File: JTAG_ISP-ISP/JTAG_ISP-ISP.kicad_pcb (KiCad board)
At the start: 2 copper layers, 23.1 x 46.1 mm, 11 parts, among them J1 Conn_02x03_Counter_Clockwise, J2 Conn_01x08, J3 Conn_01x08

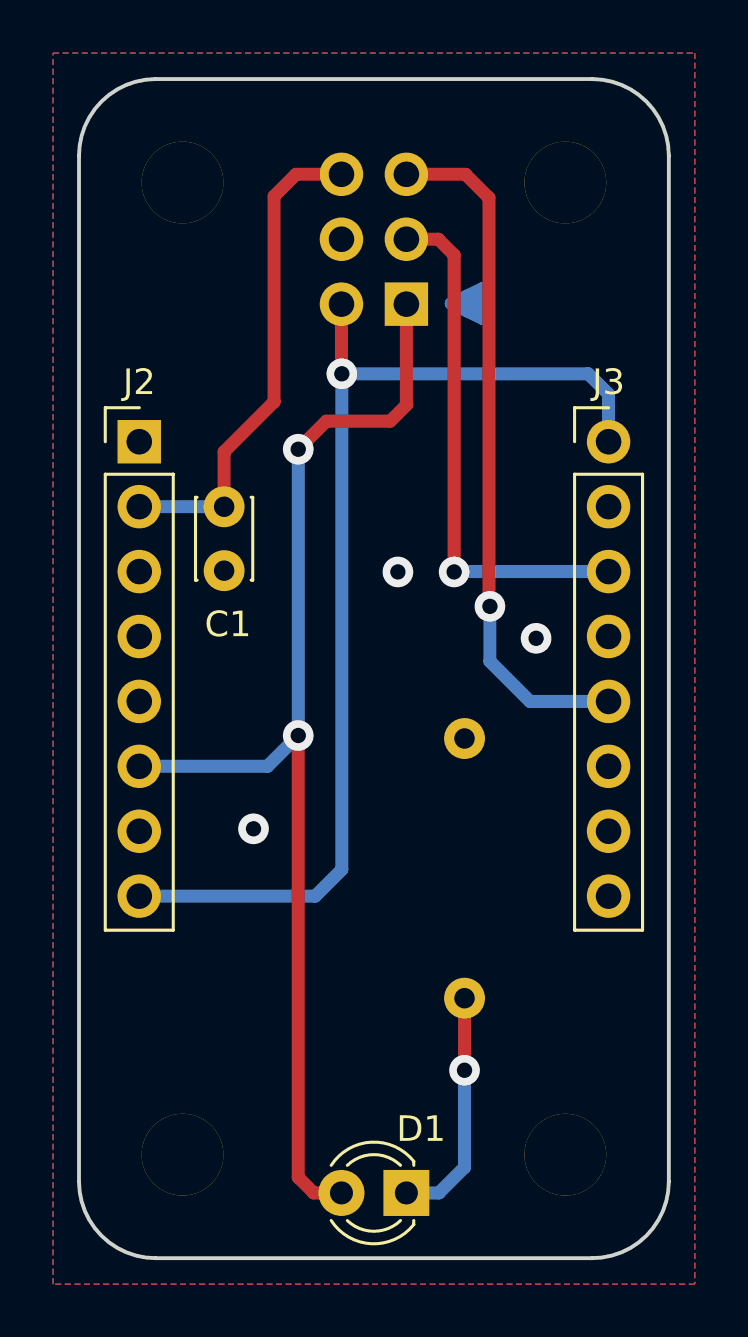
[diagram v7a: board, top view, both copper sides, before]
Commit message: # [PCB] * Correction mauvaise numérotation de broche sur le header J1 du projet ISP. * Correction de mauvaise couche pour les piste du condo C1 et de la DEL D1 du projet ISP. * Projet ISP routé à nouveau. * Utilisation de trous de montage avec pads. + Ajout de GND et de VCC dans le projet ISP sur les broches non utilisés de J2 & J3. * Mise à jours de la cartouche pour les 2 projets.     * Date actuelle;     * Version actuelle;     * Titre du projet.
# [SCHÉMA]
* Correction mauvaise numérotation de broche sur le header J1 du projet ISP.
+ Ajout de GND et de VCC dans le projet ISP sur les broches non utilisés de J2 & J3.
    + Ajout des nouveaux nom de broche sur J2 & J3.
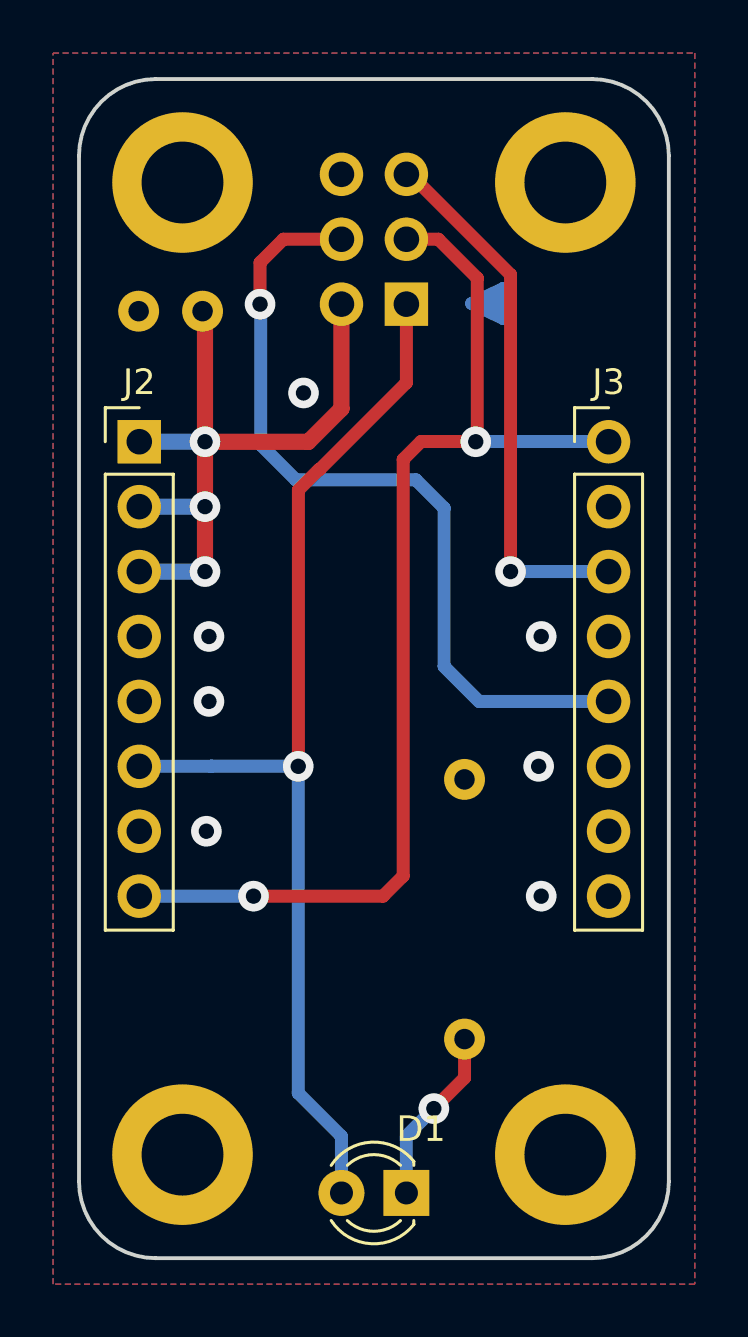
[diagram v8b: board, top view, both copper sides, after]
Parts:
- removed the REF** at (163.8, 103.4)
- removed the REF** at (163.8, 65.4)
- removed the REF** at (148.9, 103.4)
- removed the REF** at (148.9, 65.4)
- added REF**: MountingHole_3.2mm_M3_ISO14580_Pad, MountingHole:MountingHole_3.2mm_M3_ISO14580_Pad, F.Cu at (148.9, 65.4)
- added REF**: MountingHole_3.2mm_M3_ISO14580_Pad, MountingHole:MountingHole_3.2mm_M3_ISO14580_Pad, F.Cu at (148.9, 103.4)
- added REF**: MountingHole_3.2mm_M3_ISO14580_Pad, MountingHole:MountingHole_3.2mm_M3_ISO14580_Pad, F.Cu at (163.8, 65.4)
- added REF**: MountingHole_3.2mm_M3_ISO14580_Pad, MountingHole:MountingHole_3.2mm_M3_ISO14580_Pad, F.Cu at (163.8, 103.4)
- C1: moved to B.Cu
- J1: value Conn_02x03_Counter_Clockwise -> Conn_02x03_Odd_Even
- moved C1 7.70 mm to (149.7, 70.4), turned to 180 degrees
- moved R1 1.60 mm to (159.9, 98.9)
- moved REF** 0.80 mm to (161.4, 70.5)
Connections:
- J1 pad 2: SCLK -> +5V
- J1 pad 3: RESET -> SCLK
- J1 pad 4: GND -> MOSI
- J1 pad 5: MOSI -> RESET
- J1 pad 6: +5V -> GND
- J2 pad 1: unconnected-(J2-Pad1) -> +5V
- J2 pad 3: unconnected-(J2-Pad3) -> +5V
- J2 pad 5: unconnected-(J2-Pad5) -> GND
- J2 pad 7: unconnected-(J2-Pad7) -> GND
- J3 pad 2: unconnected-(J3-Pad2) -> GND
- J3 pad 4: unconnected-(J3-Pad4) -> GND
- J3 pad 6: unconnected-(J3-Pad6) -> GND
- J3 pad 8: unconnected-(J3-Pad8) -> GND
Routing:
- net +5V: track 19.3 -> 28.1 mm, vias 0 -> 3
- net MOSI: track 27.1 -> 32.1 mm
- net MISO: track 46.1 -> 43.5 mm, vias 2 -> 1
- net Net-(D1-Pad1): track 9.31 -> 6.96 mm
- net SCLK: track 43.1 -> 45.1 mm, vias 1 -> 2
- net RESET: track 20.6 -> 21.1 mm
- net GND: vias 3 -> 7
